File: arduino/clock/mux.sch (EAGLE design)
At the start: 70 parts, among them U1 SN74HC595N, U2 SN74HC595N, U3 SN74HC595N, U4 SN74HC595N

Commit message: resetting clock egle files.
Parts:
- removed CW_A, CW_C, CW_OL, CW_S, LED6, LED7, LED8: (no value), led:LEDSMT1206
- removed R30, R31, R32: 220Ω, resistor-power:RCA4050
- added T_EIGHT_, T_ELEVEN_, T_TWELVE_, T_TWO_: (no value), led:LEDSMT1206
- renumbered CW_FE to T_FIVE_, CW_I to T_THREE_, CW_W to T_FOUR_, LED3 to T_TEN, LED4 to T_NINE, LED5 to T_ELEVEN, T_FIVE to T_SEVEN_, T_SIX to P_OCLOCK, T_THREE to T_TEN_, T_TWELVE to T_NINE_, T_TWO to T_SIX_
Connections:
- removed net N$78: LED7.C, R31.2
- removed net N$79: LED8.C, R32.2
- new net N$26: PCB1.8
- new net N$30: PCB1.~11
- new net N$6: PCB1.GND.
- net CW_C: now also P_IS.C; no longer CW_C.C
- net N$10: now also P_TO.C; no longer CW_S.C
- net N$11: now also T_ELEVEN_.C; no longer P_MINUTES.C
- net N$13: now also T_TWELVE_.C; no longer P_PAST.C
- net N$14: now also T_TWO_.C; no longer P_TO.C
- net N$16: now also T_EIGHT_.C; no longer T_ONE.C
- net N$19: now also P_TEN.C; no longer P_IS.C
- net N$20: now also P_HALF.C; no longer CW_A.C
- net N$21: now also P_TWENTY.C; no longer P_TEN.C
- net N$22: now also P_FIVE.C; no longer P_HALF.C
- net N$23: now also P_MINUTES.C; no longer P_QUARTER.C
- net N$24: now also P_QUARTER.C; no longer P_TWENTY.C
- net N$29: now also T_TWO_.A; no longer P_TO.A
- net N$3: now also T_ONE.C; no longer CW_OL.C
- net N$31: now also T_EIGHT_.A; no longer T_ONE.A
- net N$32: now also T_TWELVE_.A; no longer P_PAST.A
- net N$33: now also P_TO.A; no longer CW_S.A
- net N$34: now also P_PAST.A; no longer P_FIVE.A
- net N$36: now also T_ELEVEN_.A; no longer P_MINUTES.A
- net N$38: now also T_ONE.A; no longer CW_OL.A
- net N$44: now also P_QUARTER.A; no longer P_TWENTY.A
- net N$53: now also P_IS.A; no longer CW_C.A
- net N$54: now also P_TEN.A; no longer P_IS.A
- net N$55: now also P_HALF.A; no longer CW_A.A
- net N$56: now also P_TWENTY.A; no longer P_TEN.A
- net N$57: now also P_MINUTES.A; no longer P_QUARTER.A
- net N$58: now also P_FIVE.A; no longer P_HALF.A
- net N$77: now also PCB1.12; no longer LED6.C, R30.2
- net N$80: no longer R30.1, R31.1, R32.1
- net N$84: no longer LED6.A
- net N$85: no longer LED7.A
- net N$86: no longer LED8.A
- net N$9: now also P_PAST.C; no longer P_FIVE.C
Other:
- moved on the sheet: P_FIVE, P_HALF, P_IS, P_MINUTES, P_PAST, P_QUARTER, P_TEN, P_TO, P_TWENTY, T_ONE

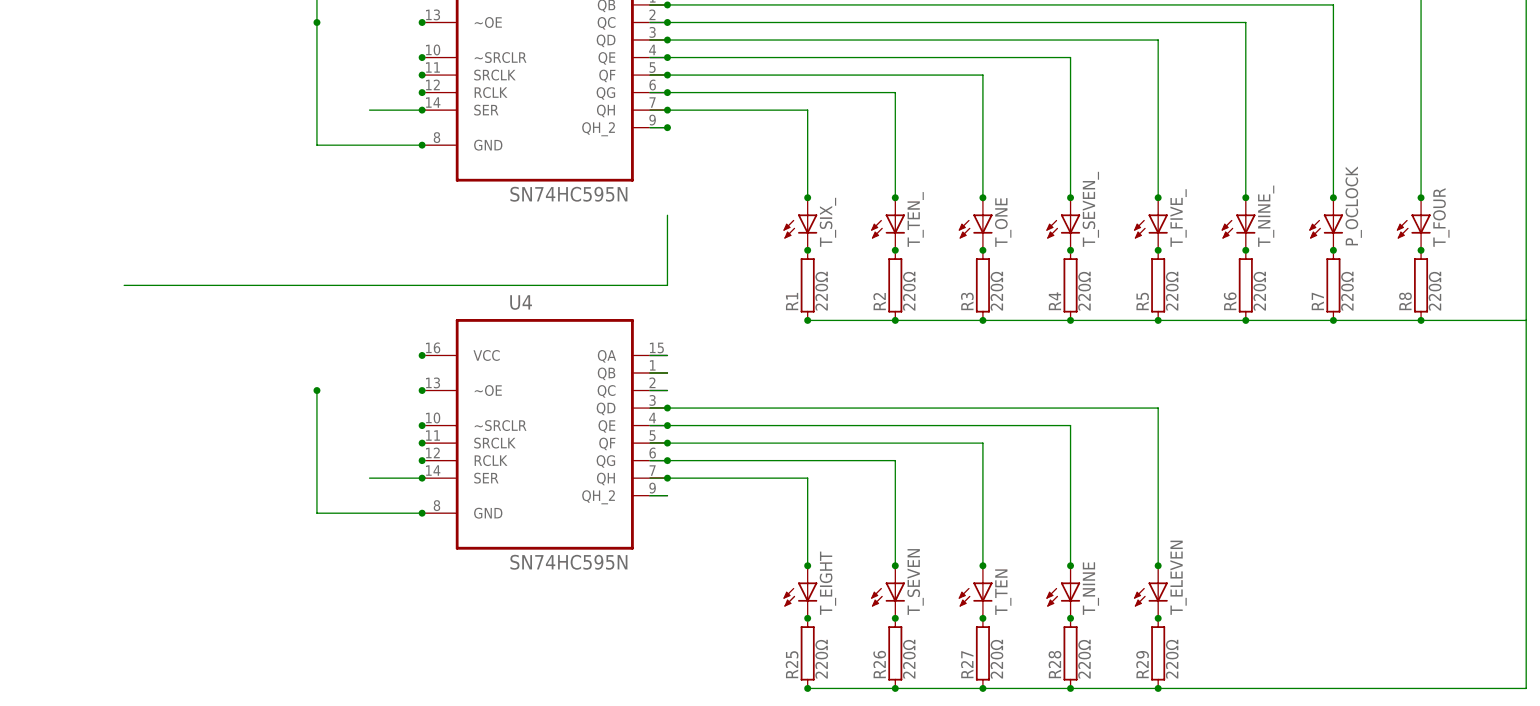
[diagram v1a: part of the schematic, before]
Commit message: Remove U3 shift register, as it is no longer needed without the CW elements.
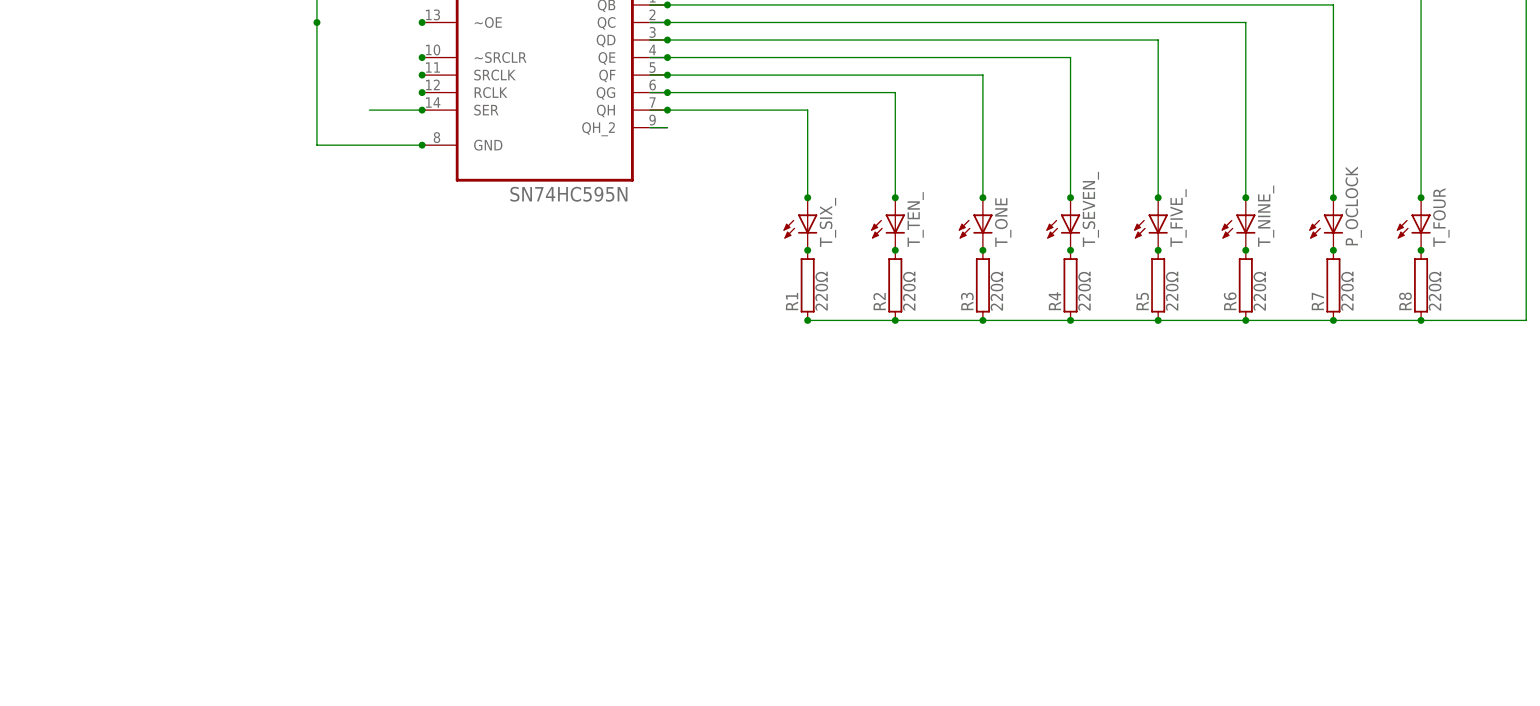
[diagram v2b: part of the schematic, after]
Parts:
- removed R25, R26, R27, R28, R29: 220Ω, resistor-power:RCA4050
- removed T_EIGHT, T_ELEVEN, T_NINE, T_SEVEN, T_TEN: (no value), led:LEDSMT1206
- removed U4: SN74HC595N, SN74HC595N:SN74HC595N
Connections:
- removed net N$18: R25.2, T_EIGHT.C
- removed net N$73: R26.2, T_SEVEN.C
- removed net N$74: R27.2, T_TEN.C
- removed net N$75: R28.2, T_NINE.C
- removed net N$76: R29.2, T_ELEVEN.C
- removed net N$81: T_SEVEN.A, U4.QG
- removed net N$82: T_TEN.A, U4.QF
- removed net N$83: T_ELEVEN.A, U4.QD
- removed net N$84: U4.QC
- removed net N$85: U4.QB
- removed net N$86: U4.QA
- removed net N$87: T_NINE.A, U4.QE
- removed net N$88: T_EIGHT.A, U4.QH
- removed net N$90: U4.QH_2
- removed net N$91: U4.VCC
- removed net N$92: U4.~OE
- removed net N$93: U4.~SRCLR
- removed net N$94: U4.SER
- removed net N$95: U4.SRCLK
- removed net N$96: U4.RCLK
- net N$80: no longer R25.1, R26.1, R27.1, R28.1, R29.1, U4.GND
